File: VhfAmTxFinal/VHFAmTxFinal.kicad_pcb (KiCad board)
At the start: 2 copper layers, 70 x 50 mm, 25 parts, among them J1 Conn_Coaxial_Small, J2 Conn_01x02, J3 Conn_Coaxial_Small, Q1 2SK3074

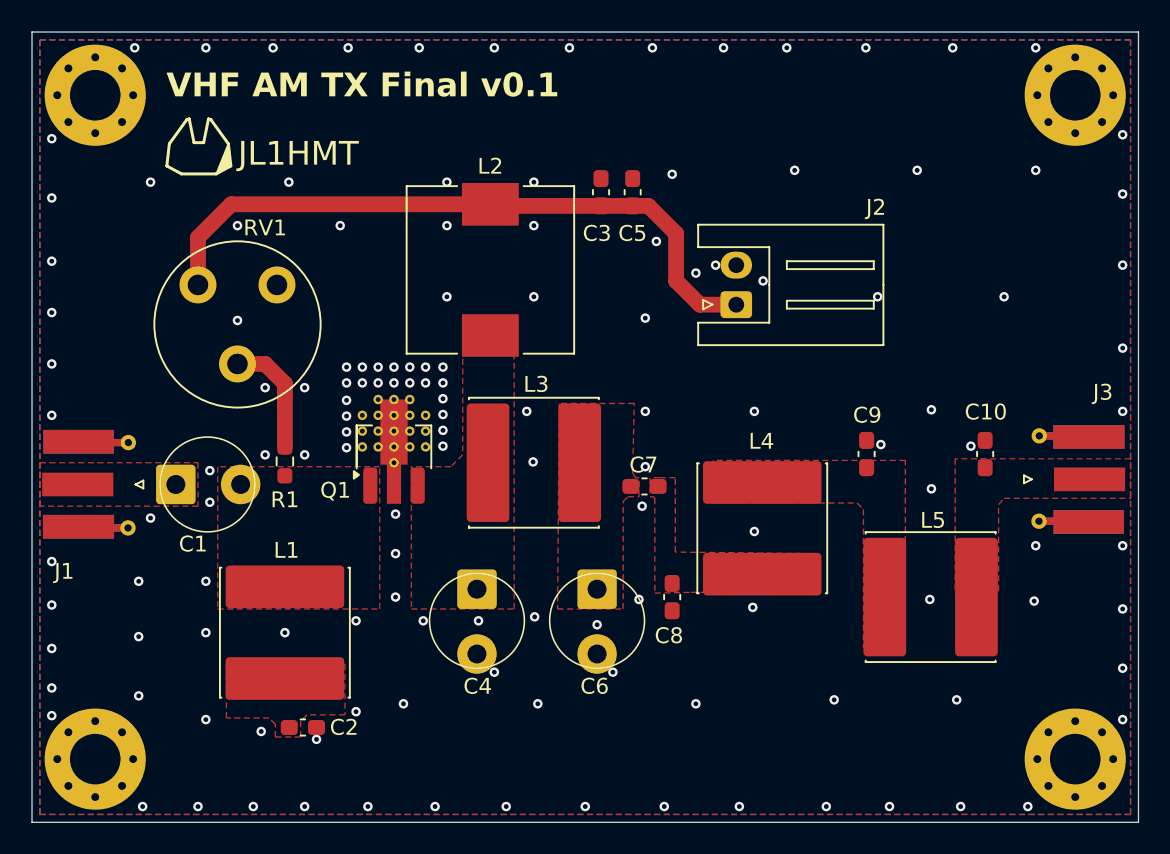
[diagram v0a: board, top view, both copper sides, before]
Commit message: バイアス電圧用調整・安全用抵抗の追加とレイアウト修正
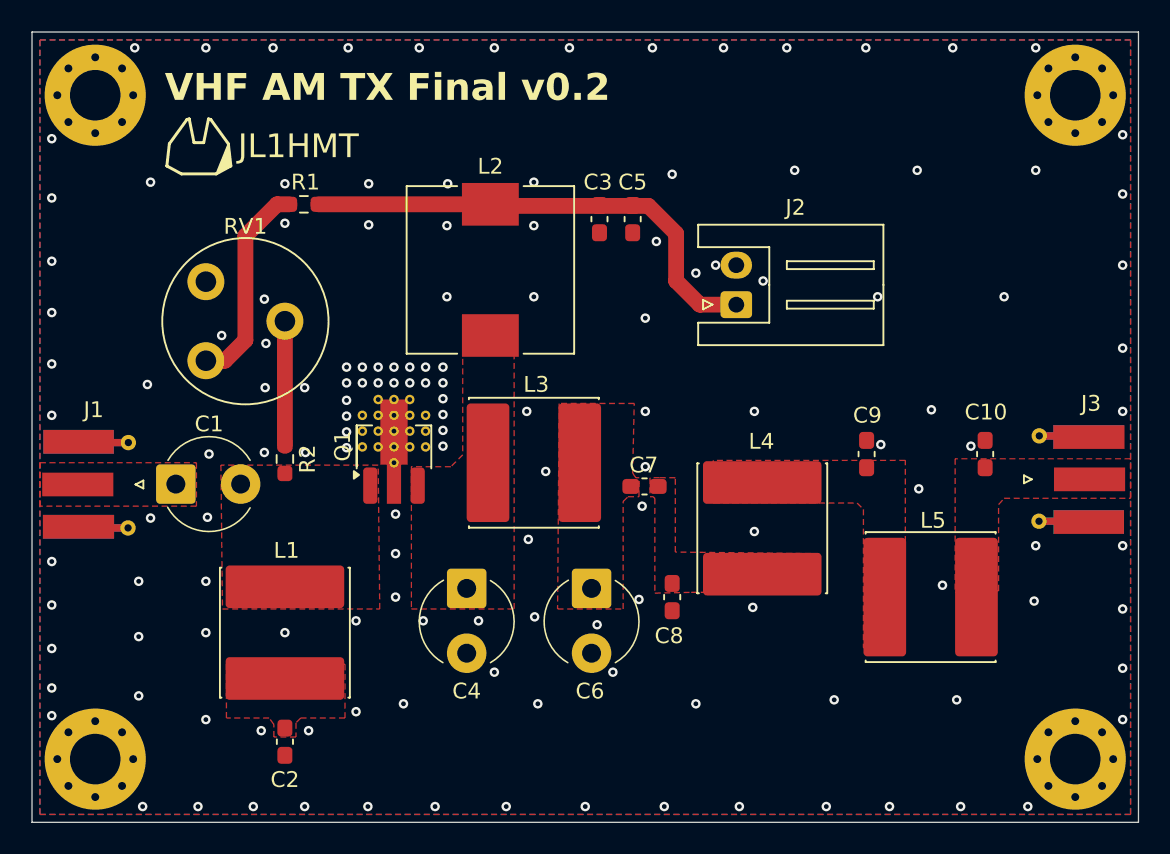
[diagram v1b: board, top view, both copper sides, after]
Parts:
- added R2: 2.2k, Resistor_SMD:R_0603_1608Metric_Pad0.98x0.95mm_HandSolder, F.Cu at (66.0, 77.0)
- C1, C4, C6: footprint ARPowerAmpLibrary:Ceramic_Trimmer_Capacitors_THT -> VHFAmTxFinalLibrary:Ceramic_Trimmer_Capacitors_THT
- J1, J3: footprint ARPowerAmpLibrary:SMA_S-063-49-TGG_EdgeMount_Horizontal -> VHFAmTxFinalLibrary:SMA_S-063-49-TGG_EdgeMount_Horizontal
- Q1: footprint ARPowerAmpLibrary:SOT-89-3_Handsoldering_Thirmo_Via -> VHFAmTxFinalLibrary:SOT-89-3_Handsoldering_Thirmo_Via
- R1: value 2.2k -> 10k
- moved R1 16.3 mm to (67.2, 60.9), turned to 0 degrees
- moved C4 4.90 mm to (77.5, 87.3)
- moved RV1 4.82 mm to (61.0, 70.8), turned to 0 degrees
- moved C6 4.67 mm to (85.4, 87.3)
- moved C1 4.44 mm to (61.2, 78.6)
- moved C3 1.70 mm to (85.9, 61.8), turned to -90 degrees
- moved C5 1.70 mm to (88.0, 61.8), turned to -90 degrees
- moved C2 1.45 mm to (66.0, 94.9), turned to -90 degrees
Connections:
- R1 pad 2: Net-(Q1-G) -> +5V
- RV1 pad 1: +5V -> Net-(R1-Pad1)
- RV1 pad 2: Net-(R1-Pad1) -> Net-(R2-Pad1)
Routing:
- net +5V: track 42.3 -> 30.8 mm
- net Net-(R2-Pad1): track 0.00 -> 7.89 mm
- net Net-(R1-Pad1): track 7.52 -> 13.3 mm
- net GND: vias 139 -> 144
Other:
- board text added: "VHF AM TX Final v0.2"
- board text removed: "VHF AM TX Final v0.1"

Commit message: HTL7G06S006Pの対応 READMEアップデート
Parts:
- added C11: 33p, Capacitor_SMD:C_0603_1608Metric_Pad1.08x0.95mm_HandSolder, F.Cu at (104.7, 76.7)
- added C12: 15p, Capacitor_SMD:C_0603_1608Metric_Pad1.08x0.95mm_HandSolder, F.Cu at (110.5, 76.8)
- C5: renamed from C4; value 30p -> 47p; footprint VHFAmTxFinalLibrary:Ceramic_Trimmer_Capacitors_THT -> Capacitor_SMD:C_0603_1608Metric_Pad1.08x0.95mm_HandSolder
- C7: value 1000p -> 30p; footprint Capacitor_SMD:C_0603_1608Metric_Pad1.08x0.95mm_HandSolder -> VHFAmTxFinalLibrary:Ceramic_Trimmer_Capacitors_THT
- C8: value 15p -> 47p
- C9: value 33p -> 1000p
- moved C10 19.8 mm to (92.8, 85.9), turned to -90 degrees
- moved C9 12.1 mm to (90.8, 78.8), turned to 0 degrees
- moved C7 6.87 mm to (88.2, 85.6), turned to -90 degrees
- moved C8 6.39 mm to (84.2, 85.1)
- moved C6 6.33 mm to (79.3, 85.6)
- moved C5 3.15 mm to (75.2, 85.2)
- moved L4 1.80 mm to (98.0, 81.3)
- moved L5 0.75 mm to (107.6, 85.7)
- moved L2 0.30 mm to (78.7, 65.0)
- renumbered C3 to C1, C5 to C2, C1 to C3, C2 to C4
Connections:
- C10 pad 1: Net-(J3-In) -> Net-(C10-Pad1)
- C6 pad 1: Net-(C6-Pad1) -> Net-(Q1-D)
- C7 pad 1: Net-(C6-Pad1) -> Net-(C7-Pad1)
- C7 pad 2: Net-(C7-Pad2) -> GND
- C8 pad 1: Net-(C7-Pad2) -> Net-(C7-Pad1)
- C9 pad 1: Net-(C9-Pad1) -> Net-(C7-Pad1)
- C9 pad 2: GND -> Net-(C10-Pad1)
- L3 pad 2: Net-(C6-Pad1) -> Net-(C7-Pad1)
- L4 pad 1: Net-(C7-Pad2) -> Net-(C10-Pad1)
- L4 pad 2: Net-(C9-Pad1) -> Net-(C11-Pad1)
- L5 pad 1: Net-(C9-Pad1) -> Net-(C11-Pad1)
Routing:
- net GND: vias 144 -> 142
- added copper zone on F.Cu, net Net-(C10-Pad1)
- added copper zone on F.Cu, net Net-(C11-Pad1)
- added copper zone on F.Cu, net Net-(C7-Pad1)
- removed copper zone on F.Cu, net Net-(C6-Pad1)
- removed copper zone on F.Cu, net Net-(C7-Pad2)
- removed copper zone on F.Cu, net Net-(C9-Pad1)

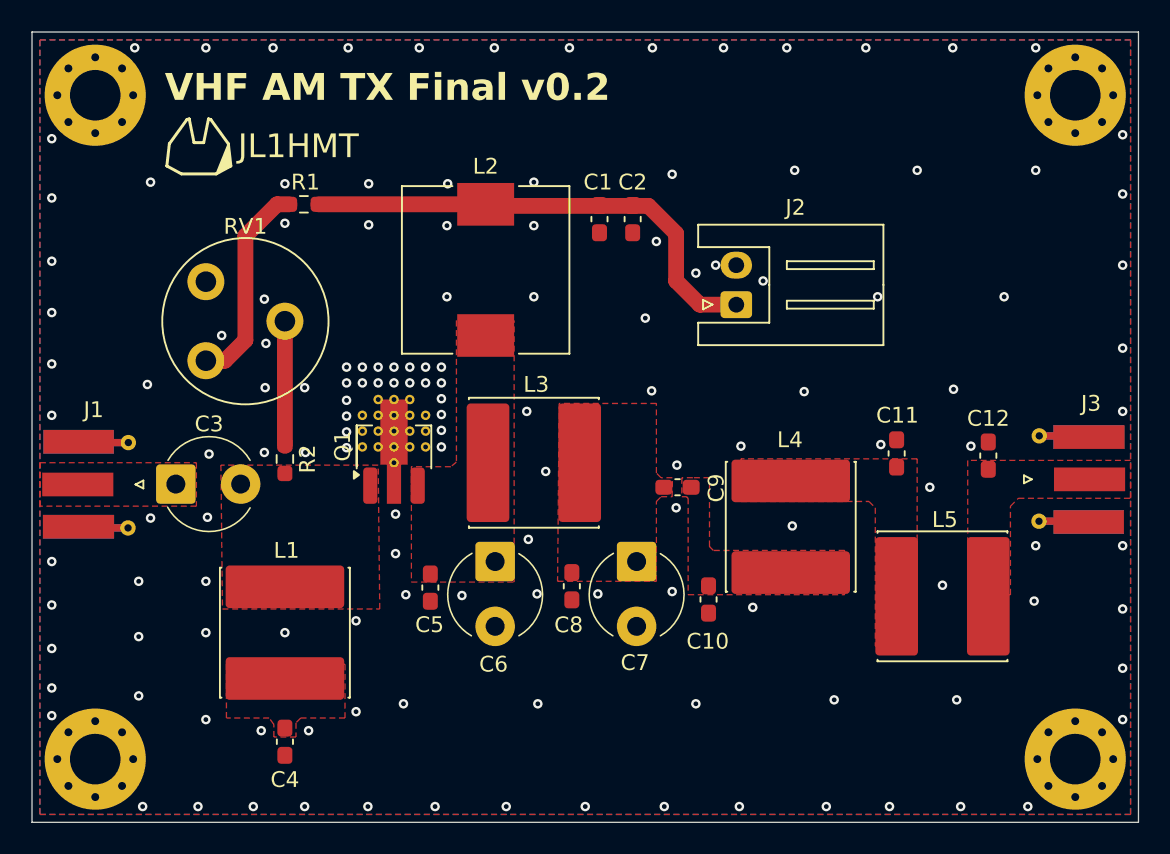
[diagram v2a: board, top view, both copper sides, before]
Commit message: 基板のレイアウト修正 v0.3
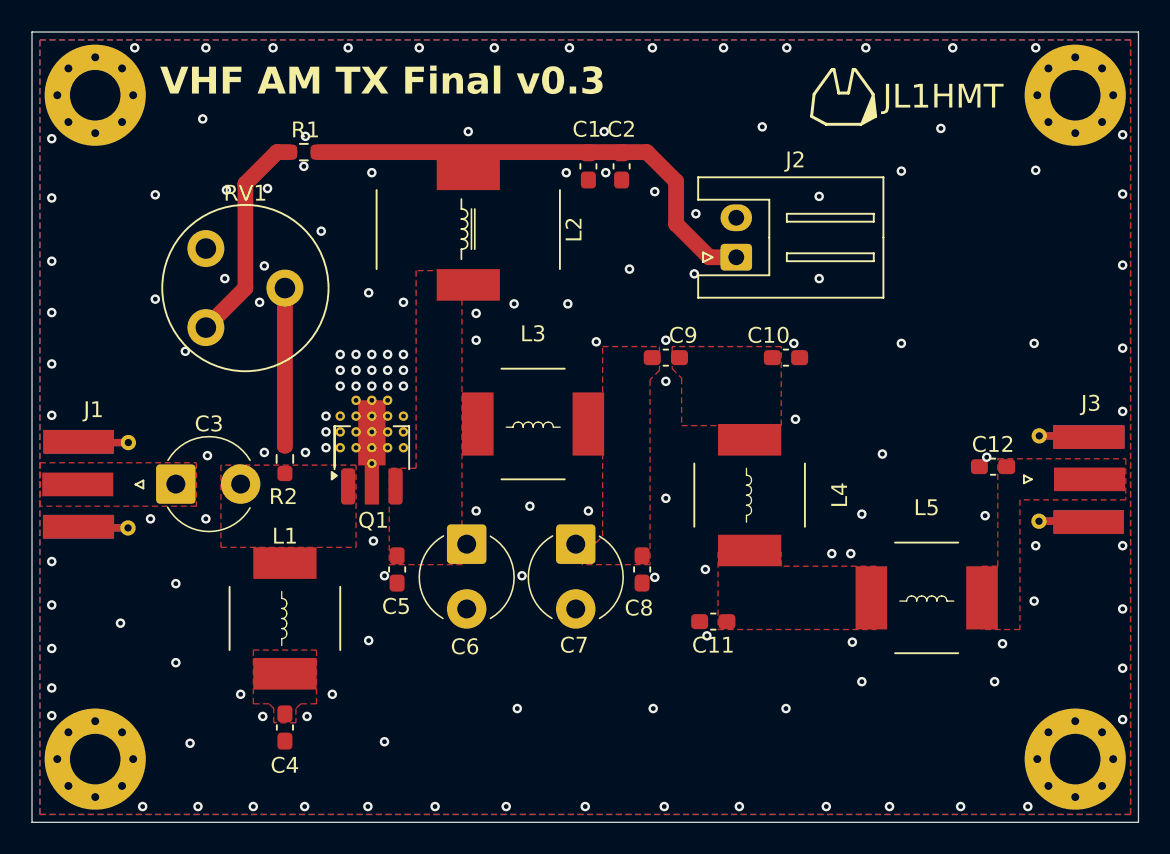
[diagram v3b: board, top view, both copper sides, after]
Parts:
- L1, L3, L4, L5: footprint Inductor_SMD:L_Cenker_CKCS8060 -> VHFAmTxFinalLibrary:Air_Core_Inductor_8mm
- L2: footprint Inductor_SMD:L_10.4x10.4_H4.8 -> VHFAmTxFinalLibrary:Choke_Inductor_10mm
- moved C10 16.1 mm to (97.7, 70.6), turned to 0 degrees
- moved C11 15.7 mm to (93.1, 87.3), turned to 180 degrees
- moved C9 8.23 mm to (90.1, 70.6)
- moved C8 4.58 mm to (88.6, 84.0)
- moved C7 4.00 mm to (84.4, 84.5)
- moved C1 3.41 mm to (85.2, 58.5)
- moved C2 3.41 mm to (87.3, 58.5)
- moved R1 3.30 mm to (67.2, 57.6)
- moved L4 3.28 mm to (95.4, 79.3), turned to -90 degrees
- moved J2 3.00 mm to (94.6, 64.2)
- moved L2 2.78 mm to (77.6, 62.5)
- moved L3 2.45 mm to (81.7, 74.8)
- moved C5 2.39 mm to (73.1, 84.0)
- moved C6 2.11 mm to (77.5, 84.5)
- moved RV1 2.09 mm to (61.0, 68.7)
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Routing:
- net Net-(R2-Pad1): track 7.89 -> 9.99 mm
- net GND: vias 142 -> 145
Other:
- board text added: "VHF AM TX Final v0.3"
- board text removed: "VHF AM TX Final v0.2"

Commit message: 基板修正
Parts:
- C8: value 47p -> 22p
- Q1: footprint VHFAmTxFinalLibrary:SOT-89-3_Handsoldering_Thirmo_Via -> Package_TO_SOT_SMD:SOT-89-3_Handsoldering
- RV1: footprint Potentiometer_THT:Potentiometer_Piher_PT-10-V05_Vertical -> Potentiometer_THT:Potentiometer_Vishay_T73YP_Vertical
- moved RV1 5.12 mm to (63.5, 64.2), turned to -90 degrees
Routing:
- net Net-(R1-Pad1): track 13.8 -> 8.24 mm
- net Net-(R2-Pad1): track 9.99 -> 9.35 mm
- net GND: vias 145 -> 148
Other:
- board text added: "VHF AM TX Final v0.4"
- board text removed: "VHF AM TX Final v0.3"
